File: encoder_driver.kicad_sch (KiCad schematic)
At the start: 31 parts, among them J4 Conn_01x02_Male, Q1 Si2319CDS

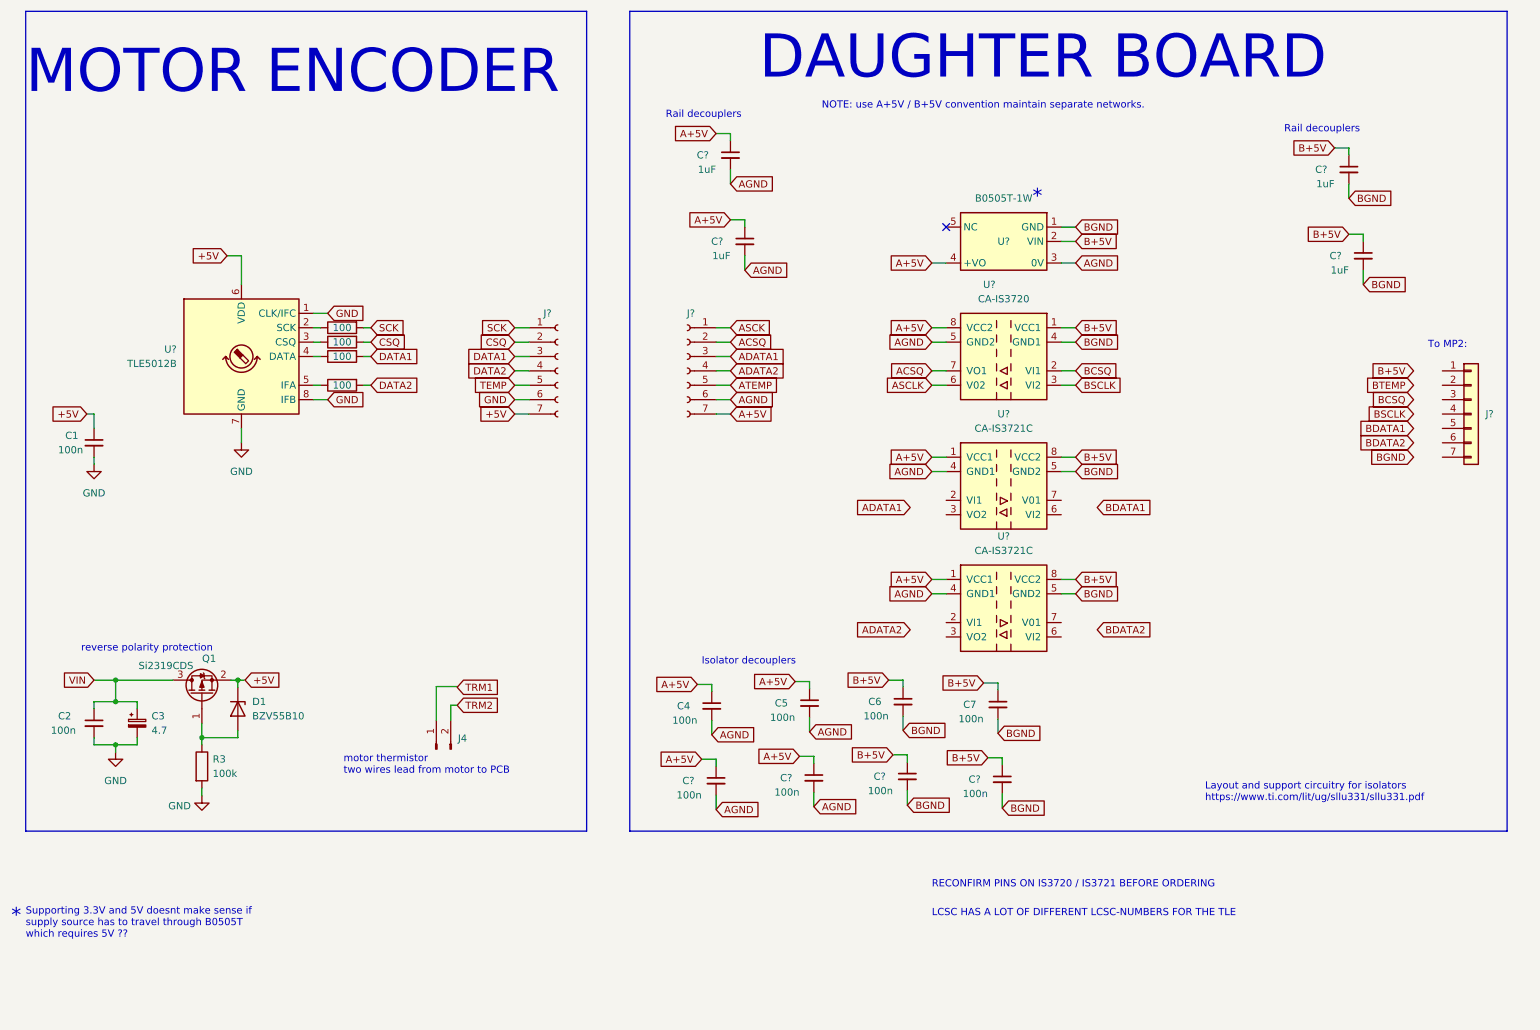
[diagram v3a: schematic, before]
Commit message: DMM Add opamp based thermistor measurement prototype Half duplex SPI option for encoder 3v3 for output to F405 board (does not like 5V on some inputs) Some component assignments to LCSC numbers
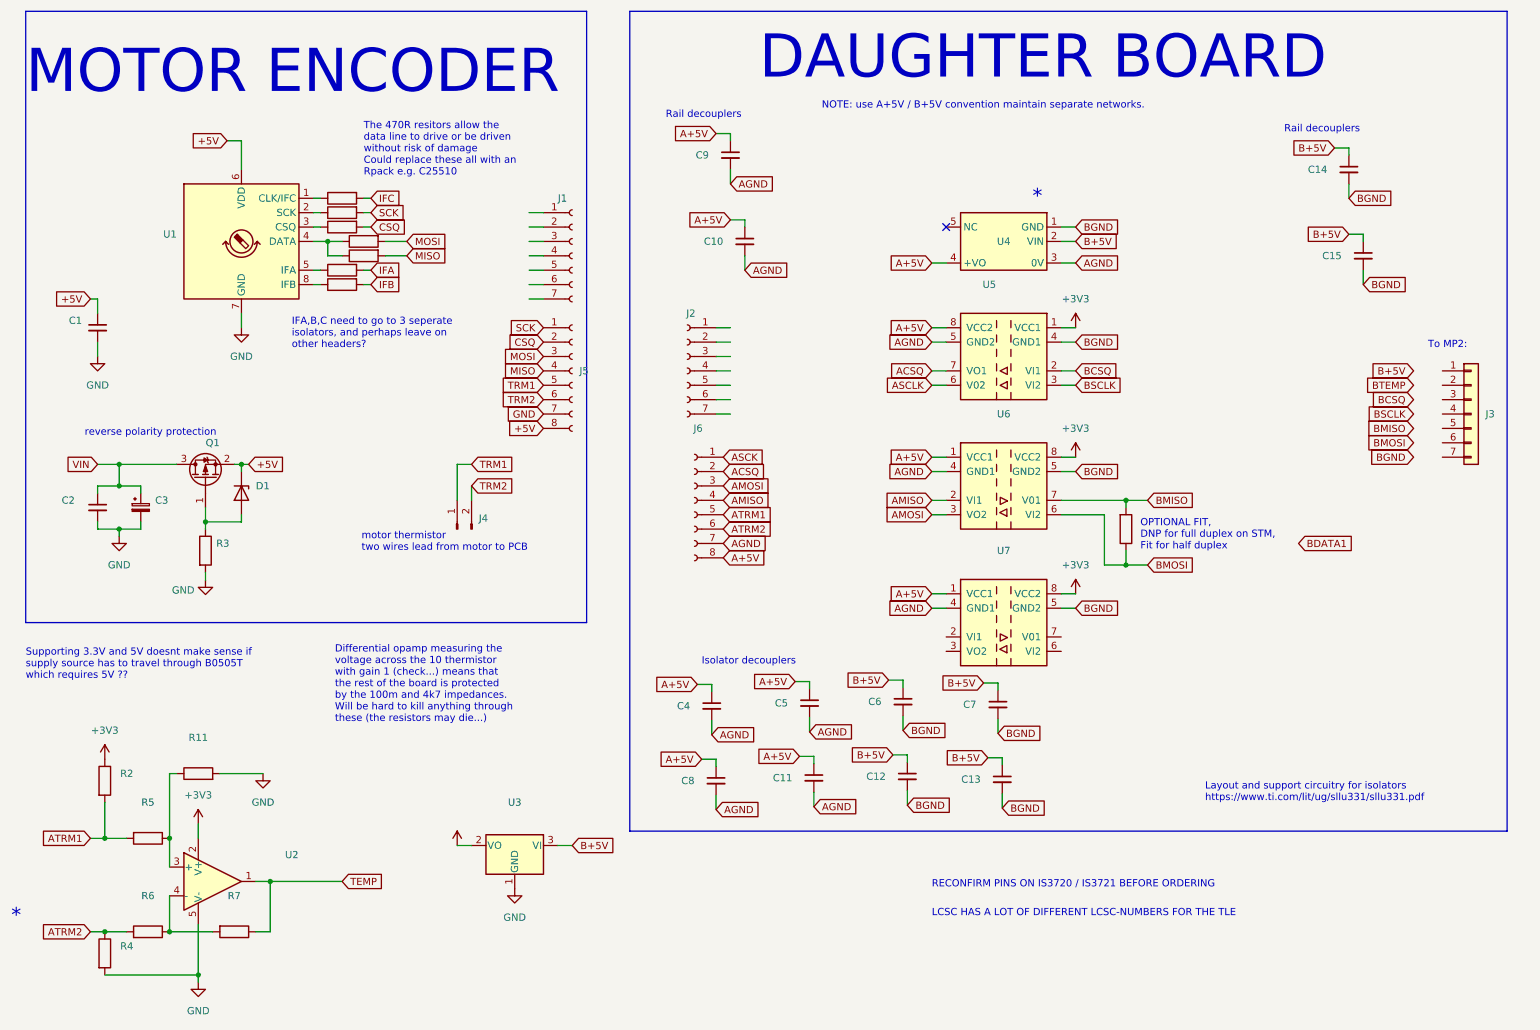
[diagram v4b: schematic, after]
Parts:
- added J5, J6: (no value), symbol Connector:Conn_01x08_Female
- added R11, R12, R13, R14, R15, R2, R4, R5, R6, R7: (no value), symbol Device:R
- added U2: (no value), symbol Amplifier_Operational:MCP6L01Rx-xOT
- added U3: (no value), symbol Regulator_Linear:XC6206PxxxMR
- C1, C2, C4, C5, C6, C7: value 100n -> (none); footprint Capacitor_SMD:C_0603_1608Metric -> (none); LCSC (none) -> C14663
- C10, C14, C15, C9: renamed from C?; value 1uF -> (none); footprint Capacitor_SMD:C_0603_1608Metric -> (none); LCSC (none) -> C15849
- C11, C12, C13, C8: renamed from C?; value 100n -> (none); footprint Capacitor_SMD:C_0603_1608Metric -> (none); LCSC (none) -> C14663
- C3: value 4.7 -> (none); footprint Capacitor_Tantalum_SMD:CP_EIA-3216-18_Kemet-A -> (none)
- D1: value BZV55B10 -> (none); footprint Diode_SMD:D_MiniMELF -> (none); LCSC (none) -> C266263
- J1, J2: renamed from J?; value Conn_01x07_Female -> (none)
- J3: renamed from J?; value Conn_01x07 -> (none)
- J4: value Conn_01x02_Male -> (none); footprint Connector_PinHeader_2.54mm:PinHeader_1x02_P2.54mm_Vertical -> (none)
- Q1: value Si2319CDS -> (none); footprint Package_TO_SOT_SMD:SOT-23 -> (none)
- R1: value 100 -> (none); footprint Resistor_SMD:R_0603_1608Metric -> (none); LCSC (none) -> C23179
- R10, R8, R9: renamed from R?; value 100 -> (none); footprint Resistor_SMD:R_0603_1608Metric -> (none); LCSC (none) -> C23179
- R3: value 100k -> (none); footprint Resistor_SMD:R_0603_1608Metric -> (none); LCSC (none) -> C25803
- U1: renamed from U?; value TLE5012B -> (none); footprint Package_SO:Infineon_PG-DSO-8-27_3.9x4.9mm_EP2.65x3mm -> (none)
- U4: renamed from U?; value B0505T-1W -> (none); footprint EASY_EDA:PWRM-SMD_B0505XT-1WR2 -> (none)
- U5: renamed from U?; value CA-IS3720 -> (none); footprint Package_SO:SOIC-8_3.9x4.9mm_P1.27mm -> (none); LCSC (none) -> C428882
- U6, U7: renamed from U?; value CA-IS3721C -> (none); footprint Package_SO:SOIC-8_3.9x4.9mm_P1.27mm -> (none); LCSC (none) -> C5121216
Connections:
- net +5V: now also J5.8 (Pin_8); no longer J1.7 (Pin_7)
- net A+5V: now also J6.8 (Pin_8); no longer J2.7 (Pin_7)
- net ACSQ: now also J6.2 (Pin_2); no longer J2.2 (Pin_2)
- net AGND: now also J6.7 (Pin_7); no longer J2.6 (Pin_6)
- net ASCK: now also J6.1 (Pin_1); no longer J2.1 (Pin_1)
- net B+5V: now also U3.3 (VI); no longer U5.1 (VCC1), U6.8 (VCC2), U7.8 (VCC2)
- net CSQ: now also J5.2 (Pin_2); no longer J1.2 (Pin_2)
- net GND: now also J5.7 (Pin_7), R11.2, R4.2, U2.5 (V-), U3.1 (GND); no longer J1.6 (Pin_6), U1.1 (CLK/IFC), U1.8 (IFB)
- net SCK: now also J5.1 (Pin_1); no longer J1.1 (Pin_1)
- net TEMP: now also R7.1, U2.1; no longer J1.5 (Pin_5)
- net TRM1: now also J4.1 (Pin_1), J5.5 (Pin_5)
- net TRM2: now also J5.6 (Pin_6)
- net AMISO: now reaches U6.2 (VI1)
- net AMISO: now also J6.4 (Pin_4)
- net AMOSI: now reaches U6.3 (VO2)
- net AMOSI: now also J6.3 (Pin_3)
- net BMOSI: now reaches U6.6 (VI2)
- net BMOSI: now also R15.1
- net BMISO: now reaches U6.7 (V01)
- net BMISO: now also R15.2
- net at R9.1, U1.4 (DATA): now also R14.1
- net ADATA1: no longer names the net of J2.3 (Pin_3)
- net ADATA2: no longer names the net of J2.4 (Pin_4)
- net ATEMP: no longer names the net of J2.5 (Pin_5)
- net DATA1: no longer names the net of J1.3 (Pin_3)
- net DATA1: no longer R9.2
- net DATA2: no longer names the net of J1.4 (Pin_4)
- net DATA2: no longer R10.2
- new net: R6.1, R7.2, U2.4 (-)
- new net: R11.1, R5.1, U2.3 (+)
- new net: R12.1, U1.1 (CLK/IFC)
- new net: R13.1, U1.8 (IFB)
- new net +3V3: R2.1, U2.2 (V+), U3.2 (VO), U5.1 (VCC1), U6.8 (VCC2), U7.8 (VCC2)
- new net ATRM1: J6.5 (Pin_5), R2.2, R5.2
- new net ATRM2: J6.6 (Pin_6), R4.1, R6.2
- new net IFA: R10.2
- new net IFB: R13.2
- new net IFC: R12.2
- new net MISO: J5.4 (Pin_4), R14.2
- new net MOSI: J5.3 (Pin_3), R9.2
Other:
- note added: "Differential opamp measuring the voltage across the 10 thermistor with gain 1 (check...) means that the rest of the board is protected by the 100m and 4k7 impedances. Will be hard to kill anything through these (the resistors may die...)"
- note added: "IFA,B,C need to go to 3 seperate isolators, and perhaps leave on other headers?"
- note added: "OPTIONAL FIT, DNP for full duplex on STM, Fit for half duplex"
- note added: "The 470R resitors allow the data line to drive or be driven without risk of damage Could replace these all with an Rpack e.g. C25510"
- moved on the sheet: C1, C2, C3, D1, J1, J4, Q1, R3, U1, U7
